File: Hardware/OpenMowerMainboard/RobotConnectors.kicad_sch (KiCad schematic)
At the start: 27 parts, among them IC1 74ALVC164245DGG,11, J1 Conn_02x11_Top_Bottom, J10 Conn_01x05, J11 Conn_01x03_Male, J12 Conn_01x03_Male, J13 Conn_01x03_Male, J14 Conn_01x03_Male, J17 Conn_01x02, J18 Conn_01x02, J19 Conn_01x04, J2 Conn_02x04_Top_Bottom, J3 Conn_01x02, J4 Conn_01x05, J5 Conn_01x04, J6 Conn_01x04, J7 Conn_01x04, J8 Conn_01x04, J9 Conn_01x04

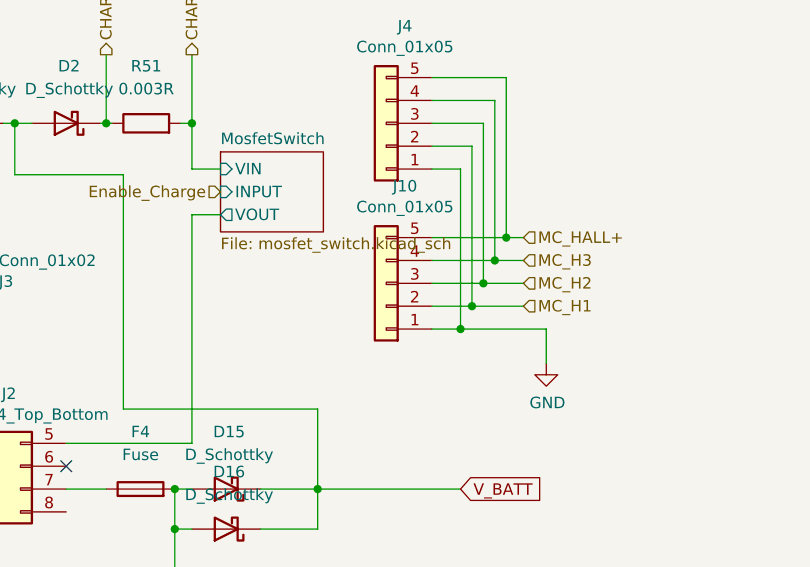
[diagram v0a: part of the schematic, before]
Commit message: fix(motorsensor): J10 was upside-down
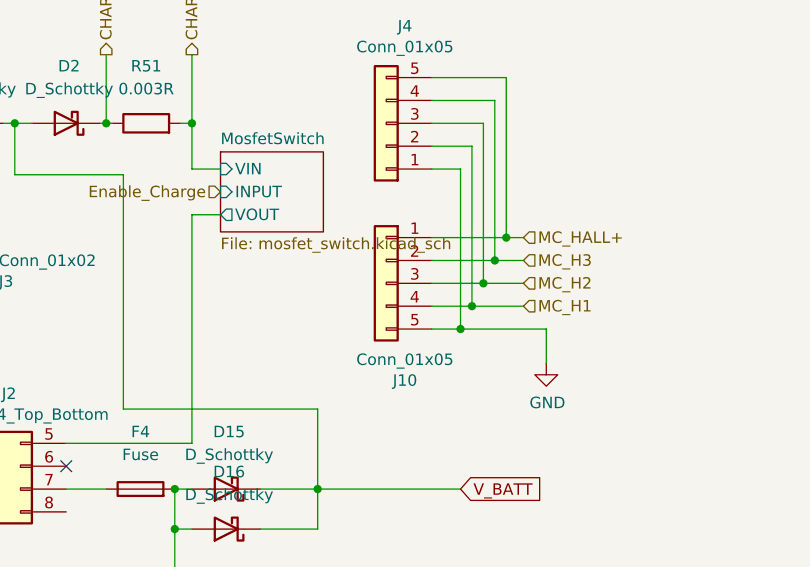
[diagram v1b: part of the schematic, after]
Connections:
- net GND: now also J10.5 (Pin_5); no longer J10.1 (Pin_1)
- net MC_H1: now also J10.4 (Pin_4); no longer J10.2 (Pin_2)
- net MC_H3: now also J10.2 (Pin_2); no longer J10.4 (Pin_4)
- net MC_HALL+: now also J10.1 (Pin_1); no longer J10.5 (Pin_5)
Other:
- moved on the sheet: J10
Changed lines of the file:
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@@
     (pin "1")
   )
-  (symbol (lib_id "Connector_Generic:Conn_01x05") (at 146.05 45.72 180) (unit 1)
+  (symbol (lib_id "Connector_Generic:Conn_01x05") (at 146.05 45.72 0) (mirror y) (unit 1)
     (in_bom yes) (on_board yes)
-    (property "Reference" "J10" (id 0) (at 148.1328 34.925 0))
-    (property "Value" "Conn_01x05" (id 1) (at 148.1328 37.2364 0))
+    (property "Reference" "J10" (id 0) (at 148.1328 56.515 0))
+    (property "Value" "Conn_01x05" (id 1) (at 148.1328 54.2036 0))
     (property "Footprint" "Connector_JST:JST_PH_B5B-PH-K_1x05_P2.00mm_Vertical" (id 2) (at 146.05 45.72 0)
       (effects (font (size 1.27 1.27)) hide)

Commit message: feat(bom): added compatible lcsc codes, updated discontinued ones
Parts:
- D15, D16, D2, D3: LCSC (none) -> C113939
- F2, F4: Digikey FC-202-24-ND -> (none); Part Number FC-202-24 -> https://aliexpress.com/item/4000318714025.html
- IC1: LCSC (none) -> C5531
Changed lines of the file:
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@@
+      (effects (font (size 1.27 1.27)) hide)
+    )
+    (property "LCSC" "C5531" (id 13) (at 138.43 100.965 0)
       (effects (font (size 1.27 1.27)) hide)
     )
@@
       (effects (font (size 1.27 1.27)) hide)
     )
-    (property "Digikey" "FC-202-24-ND" (id 4) (at 118.745 68.58 0)
-      (effects (font (size 1.27 1.27)) hide)
-    )
-    (property "Part Number" "FC-202-24" (id 5) (at 118.745 68.58 0)
+    (property "Digikey" "" (id 4) (at 118.745 68.58 0)
+      (effects (font (size 1.27 1.27)) hide)
+    )
+    (property "Part Number" "https://aliexpress.com/item/4000318714025.html" (id 5) (at 118.745 68.58 0)
       (effects (font (size 1.27 1.27)) hide)
     )
     (property "Stock_PN" "FH-FC-202-24" (id 6) (at 118.745 68.58 0)
+      (effects (font (size 1.27 1.27)) hide)
+    )
+    (property "Description" "You will need a pair of holders" (id 7) (at 118.745 68.58 0)
       (effects (font (size 1.27 1.27)) hide)
     )
@@
       (effects (font (size 1.27 1.27)) hide)
     )
+    (property "LCSC" "C113939" (id 7) (at 128.27 68.58 0)
+      (effects (font (size 1.27 1.27)) hide)
+    )
     (pin "1")
     (pin "2")
@@
       (effects (font (size 1.27 1.27)) hide)
     )
+    (property "LCSC" "C113939" (id 7) (at 128.27 73.025 0)
+      (effects (font (size 1.27 1.27)) hide)
+    )
     (pin "1")
     (pin "2")
@@
       (effects (font (size 1.27 1.27)) hide)
     )
+    (property "LCSC" "C113939" (id 7) (at 110.49 27.94 0)
+      (effects (font (size 1.27 1.27)) hide)
+    )
     (pin "1")
     (pin "2")
@@
       (effects (font (size 1.27 1.27)) hide)
     )
-    (property "Digikey" "FC-202-24-ND" (id 4) (at 94.615 33.02 0)
-      (effects (font (size 1.27 1.27)) hide)
-    )
-    (property "Part Number" "FC-202-24" (id 5) (at 94.615 33.02 0)
+    (property "Digikey" "" (id 4) (at 94.615 33.02 0)
+      (effects (font (size 1.27 1.27)) hide)
+    )
+    (property "Part Number" "https://aliexpress.com/item/4000318714025.html" (id 5) (at 94.615 33.02 0)
       (effects (font (size 1.27 1.27)) hide)
     )
     (property "Stock_PN" "FH-FC-202-24" (id 6) (at 94.615 33.02 0)
+      (effects (font (size 1.27 1.27)) hide)
+    )
+    (property "Description" "You will need a pair of holders" (id 7) (at 94.615 33.02 0)
+      (effects (font (size 1.27 1.27)) hide)
+    )
+    (property "LCSC" "" (id 8) (at 94.615 33.02 0)
       (effects (font (size 1.27 1.27)) hide)
     )
@@
       (effects (font (size 1.27 1.27)) hide)
     )
+    (property "LCSC" "C113939" (id 7) (at 99.695 27.94 0)
+      (effects (font (size 1.27 1.27)) hide)
+    )

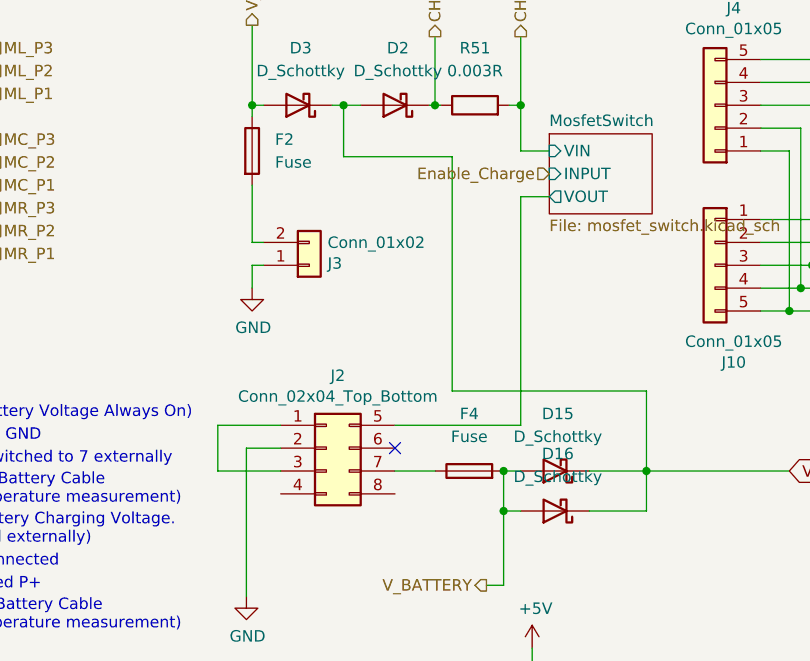
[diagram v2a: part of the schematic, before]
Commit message: fix: fixed ERC/DRC errors, removed LM2596S
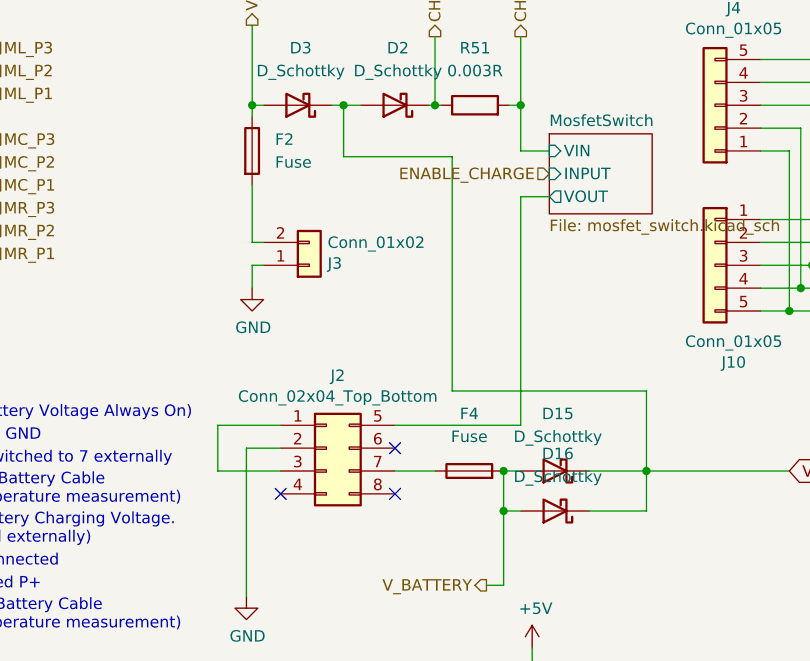
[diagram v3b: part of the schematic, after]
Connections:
- no-connect marks 8 -> 10
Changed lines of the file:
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@@
   (no_connect (at 176.53 126.365))
   (no_connect (at 176.53 121.285))
+  (no_connect (at 110.49 71.12))
+  (no_connect (at 97.79 71.12))
   (no_connect (at 110.49 66.04))
   (wire (pts (xy 242.57 76.2) (xy 240.03 76.2))
@@
     (effects (font (size 1.27 1.27)) (justify right))
   )
-  (hierarchical_label "Enable_Charge" (shape input) (at 127.635 35.56 180)
+  (hierarchical_label "ENABLE_CHARGE" (shape input) (at 127.635 35.56 180)
     (effects (font (size 1.27 1.27)) (justify right))
   )

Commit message: fix(motorsensor): replace PN for J10 with C442247
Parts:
- J10: Digikey 455-1707-ND -> (none); LCSC (none) -> C442247; Part Number B5B-PH-K-S(LF)(SN) -> (none)
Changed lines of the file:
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@@
       (effects (font (size 1.27 1.27)) hide)
     )
-    (property "Datasheet" "~" (id 3) (at 146.05 45.72 0)
-      (effects (font (size 1.27 1.27)) hide)
-    )
-    (property "Digikey" "455-1707-ND" (id 4) (at 146.05 45.72 0)
-      (effects (font (size 1.27 1.27)) hide)
-    )
-    (property "Part Number" "	B5B-PH-K-S(LF)(SN)" (id 5) (at 146.05 45.72 0)
+    (property "Datasheet" "" (id 3) (at 146.05 45.72 0)
       (effects (font (size 1.27 1.27)) hide)
     )
@@
       (effects (font (size 1.27 1.27)) hide)
     )
+    (property "LCSC" "C442247" (id 5) (at 146.05 45.72 0)
+      (effects (font (size 1.27 1.27)) hide)
+    )
